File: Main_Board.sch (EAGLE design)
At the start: 54 parts, among them U1 RN4020RN4020, U2 LMS8117, Y1 MC-30632.768K-E3, Y2 MA-5066-25.0000M-C0

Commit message: added jtag
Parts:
- added L1: (no value), SparkFun-Passives:INDUCTOR0805
- added U$11: 1000uF, BB8:CAP_POL_PAN
- added U$12: JTAG, BB8:JTAG
- added U$8: 100uF, BB8:CAP_POL_PAN
- added U3: 5V_BUCK_REG, BB8:5V_BUCK_REG
- added Z1: SCHOTTKY_DIODE, BB8:SCHOTTKY_DIODE
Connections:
- new net N$31: L1.2, U3.OUTPUT, Z1.C
- new net N$32: L1.1, U$11.+, U3.FEEDBACK
- net GND: now also U$11.-, U$8.-, U3.!ON/OFF, U3.GND, Z1.A
- net VCC: now also U$8.+, U3.VIN
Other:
- note added: "double check"
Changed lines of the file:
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@@
 <part name="FRAME4" library="SparkFun-Aesthetics" deviceset="FRAME-LEDGER" device=""/>
 <part name="U2" library="BB8" deviceset="LMS8117" device=""/>
+<part name="U3" library="BB8" deviceset="5V_BUCK_REG" device=""/>
+<part name="SUPPLY20" library="SparkFun-Aesthetics" deviceset="VCC" device=""/>
+<part name="GND32" library="SparkFun-Aesthetics" deviceset="GND" device=""/>
+<part name="U$8" library="BB8" deviceset="CAP_POL_PAN" device="" value="100uF"/>
+<part name="Z1" library="BB8" deviceset="SCHOTTKY_DIODE" device=""/>
+<part name="L1" library="SparkFun-Passives" deviceset="INDUCTOR" device="0805"/>
+<part name="U$11" library="BB8" deviceset="CAP_POL_PAN" device="" value="1000uF"/>
+<part name="GND34" library="SparkFun-Aesthetics" deviceset="GND" device=""/>
+<part name="GND35" library="SparkFun-Aesthetics" deviceset="GND" device=""/>
+<part name="U$12" library="BB8" deviceset="JTAG" device=""/>
 </parts>
 <sheets>
@@
 MC1_INH_3.3
 MC2_INH_3.3</text>
+<text x="35.56" y="-187.96" size="1.778" layer="95">double check</text>
 </plain>
 <instances>
@@
 <instance part="FRAME4" gate="G$2" x="154.94" y="-43.18"/>
 <instance part="U2" gate="G$1" x="-104.14" y="-93.98"/>
+<instance part="U3" gate="G$1" x="-45.72" y="-180.34"/>
+<instance part="SUPPLY20" gate="G$1" x="-76.2" y="-175.26"/>
+<instance part="GND32" gate="1" x="-76.2" y="-208.28"/>
+<instance part="U$8" gate="G$1" x="-101.6" y="-180.34"/>
+<instance part="Z1" gate="G$1" x="-10.16" y="-187.96" rot="R90"/>
+<instance part="L1" gate="G$1" x="5.08" y="-185.42" rot="MR90"/>
+<instance part="U$11" gate="G$1" x="25.4" y="-190.5"/>
+<instance part="GND34" gate="1" x="-10.16" y="-208.28"/>
+<instance part="GND35" gate="1" x="25.4" y="-208.28"/>
+<instance part="U$12" gate="G$1" x="528.32" y="60.96"/>
 </instances>
 <busses>
@@
 <wire x1="7.62" y1="50.8" x2="7.62" y2="48.26" width="0.1524" layer="91"/>
 </segment>
+<segment>
+<pinref part="SUPPLY20" gate="G$1" pin="VCC"/>
+<pinref part="U3" gate="G$1" pin="VIN"/>
+<wire x1="-76.2" y1="-175.26" x2="-76.2" y2="-177.8" width="0.1524" layer="91"/>
+<wire x1="-76.2" y1="-177.8" x2="-60.96" y2="-177.8" width="0.1524" layer="91"/>
+<junction x="-76.2" y="-177.8"/>
+<pinref part="U$8" gate="G$1" pin="+"/>
+<wire x1="-76.2" y1="-177.8" x2="-101.6" y2="-177.8" width="0.1524" layer="91"/>
+</segment>
 </net>
 <net name="GND" class="0">
@@
 <wire x1="304.8" y1="177.8" x2="304.8" y2="175.26" width="0.1524" layer="91"/>
 <pinref part="JP1" gate="G$1" pin="O"/>
+</segment>
+<segment>
+<pinref part="U3" gate="G$1" pin="!ON/OFF"/>
+<pinref part="GND32" gate="1" pin="GND"/>
+<wire x1="-60.96" y1="-182.88" x2="-76.2" y2="-182.88" width="0.1524" layer="91"/>
+<wire x1="-76.2" y1="-182.88" x2="-76.2" y2="-187.96" width="0.1524" layer="91"/>
+<pinref part="U3" gate="G$1" pin="GND"/>
+<wire x1="-76.2" y1="-187.96" x2="-76.2" y2="-205.74" width="0.1524" layer="91"/>
+<wire x1="-60.96" y1="-187.96" x2="-76.2" y2="-187.96" width="0.1524" layer="91"/>
+<junction x="-76.2" y="-187.96"/>
+<pinref part="U$8" gate="G$1" pin="-"/>
+<wire x1="-76.2" y1="-187.96" x2="-101.6" y2="-187.96" width="0.1524" layer="91"/>
+<wire x1="-101.6" y1="-187.96" x2="-101.6" y2="-185.42" width="0.1524" layer="91"/>
+</segment>
+<segment>
+<pinref part="Z1" gate="G$1" pin="A"/>
+<pinref part="GND34" gate="1" pin="GND"/>
+<wire x1="-10.16" y1="-203.2" x2="-10.16" y2="-205.74" width="0.1524" layer="91"/>
+</segment>
+<segment>
+<pinref part="GND35" gate="1" pin="GND"/>
+<wire x1="25.4" y1="-205.74" x2="25.4" y2="-195.58" width="0.1524" layer="91"/>
+<pinref part="U$11" gate="G$1" pin="-"/>
 </segment>
 </net>
@@
 </segment>
 </net>
+<net name="N$31" class="0">
+<segment>
+<pinref part="U3" gate="G$1" pin="OUTPUT"/>
+<pinref part="L1" gate="G$1" pin="2"/>
+<wire x1="-30.48" y1="-185.42" x2="-10.16" y2="-185.42" width="0.1524" layer="91"/>
+<pinref part="Z1" gate="G$1" pin="C"/>
+<wire x1="-10.16" y1="-185.42" x2="-2.54" y2="-185.42" width="0.1524" layer="91"/>
+<wire x1="-10.16" y1="-187.96" x2="-10.16" y2="-185.42" width="0.1524" layer="91"/>
+<junction x="-10.16" y="-185.42"/>
+</segment>
+</net>
+<net name="N$32" class="0">
+<segment>
+<pinref part="L1" gate="G$1" pin="1"/>
+<pinref part="U$11" gate="G$1" pin="+"/>
+<wire x1="12.7" y1="-185.42" x2="25.4" y2="-185.42" width="0.1524" layer="91"/>
+<wire x1="25.4" y1="-185.42" x2="25.4" y2="-187.96" width="0.1524" layer="91"/>
+<pinref part="U3" gate="G$1" pin="FEEDBACK"/>
+<wire x1="-30.48" y1="-177.8" x2="25.4" y2="-177.8" width="0.1524" layer="91"/>
+<wire x1="25.4" y1="-177.8" x2="25.4" y2="-185.42" width="0.1524" layer="91"/>
+<junction x="25.4" y="-185.42"/>
+</segment>
+</net>

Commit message: started adding motors
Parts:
- added J1: (no value), SparkFun-Connectors:M03PTH
- added LED1, LED2, LED3: (no value), LilyPad-Wearables:LED1206
- added R16, R17, R18, R19, R20, R21, R22, R23, R24: 10K, SparkFun-Passives:RESISTOR0805-RES
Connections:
- new net !NRST: S2.O, U$12.NRST, U$5.!RST
- new net BLUE_WAKE_SW: U$5.PA4, U1.WAKE_SW
- new net BLU_CTS: U$5.PA1, U1.PIO5
- new net BLU_RTS: U$5.PA0_WKUP, U1.RTS/PIO6
- new net BLU_RX: U$5.PA2, U1.UART_RX
- new net BLU_TX: U$5.PA3, U1.UART_TX
- new net BLU_WAKE_HW: U$5.PA6, U1.WAKE_HW
- new net JNTRST: U$12.JNTRST, U$5.PB4
- new net JTCK: U$12.JTCK, U$5.PA14
- new net JTDI: U$12.JTDI, U$5.PA15
- new net JTDO: U$12.JTDO, U$5.PB3
- new net JTMS: U$12.JTMS, U$5.PA13
- new net N$33: U1.CMD/MLDP
- new net N$34: R22.2, U1.PIO1
- new net N$35: LED1.A, R22.1
- new net N$36: R23.2, U1.PIO2
- new net N$37: R24.2, U1.PIO3
- new net N$38: LED2.A, R23.1
- new net N$39: LED3.A, R24.1
- new net SERVO_PWM_3.3: U$10.3A, U$5.PA8
- new net SERVO_PWM_5: U$10.3Y
- net 3.3V: now also U$12.VDD, U$12.VDD@2
- net 5V: no longer U$10.3!OE
- net GND: now also LED1.C, LED2.C, LED3.C, R16.1, R17.1, R18.1, R19.1, R20.1, R21.1, U$10.3!OE, U$12.GND, U$12.GND@10, U$12.GND@12, U$12.GND@14, U$12.GND@16, U$12.GND@18, U$12.GND@20, U$12.GND@6, U$12.GND@8; no longer U$10.3A
- net M1_A_3.3: now also U$5.PA7
- net M1_B_3.3: now also U$5.PC4
- net M2_A_3.3: now also U$5.PC5
- net M2_B_3.3: now also U$5.PB0
- net MC1_INH_3.3: now also U$5.PC9
- net MC2_IS: now also U$5.PC1
- net N$24: now also R16.2, U$12.P$11; no longer U$5.PA13
- net N$25: now also R17.2, U$12.P$17; no longer U$5.PA14
- net N$26: now also R18.2, U$12.P$19; no longer U$5.PA15
- net N$27: now also R20.2, U1.AIO1; no longer U$5.PB3
- net N$28: now also R21.2, U1.AIO0; no longer U$5.PB4
- net N$7: now also R19.2, U1.AIO2; no longer S2.O, U$5.!RST
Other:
- note added: "OUTPUT FROM MICRO MC1_IN1 MC1_IN2 MC2_IN1 MC2_IN2"
- moved on the sheet: S2

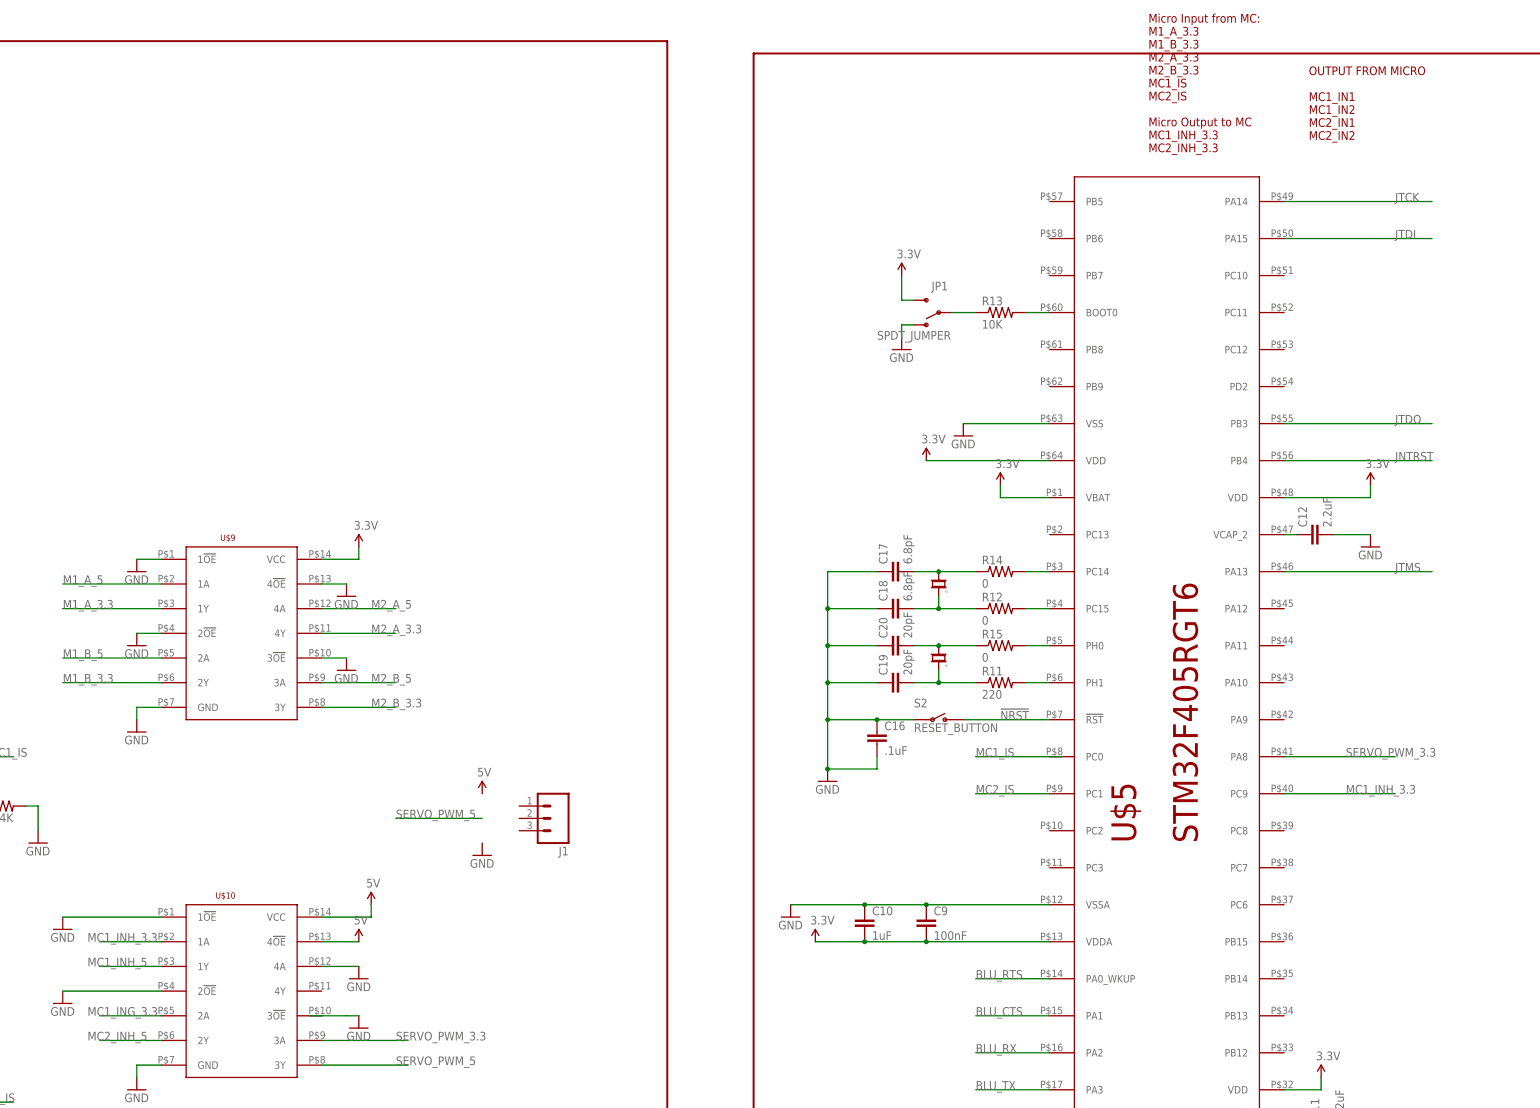
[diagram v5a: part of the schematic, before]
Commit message: finished adding motors
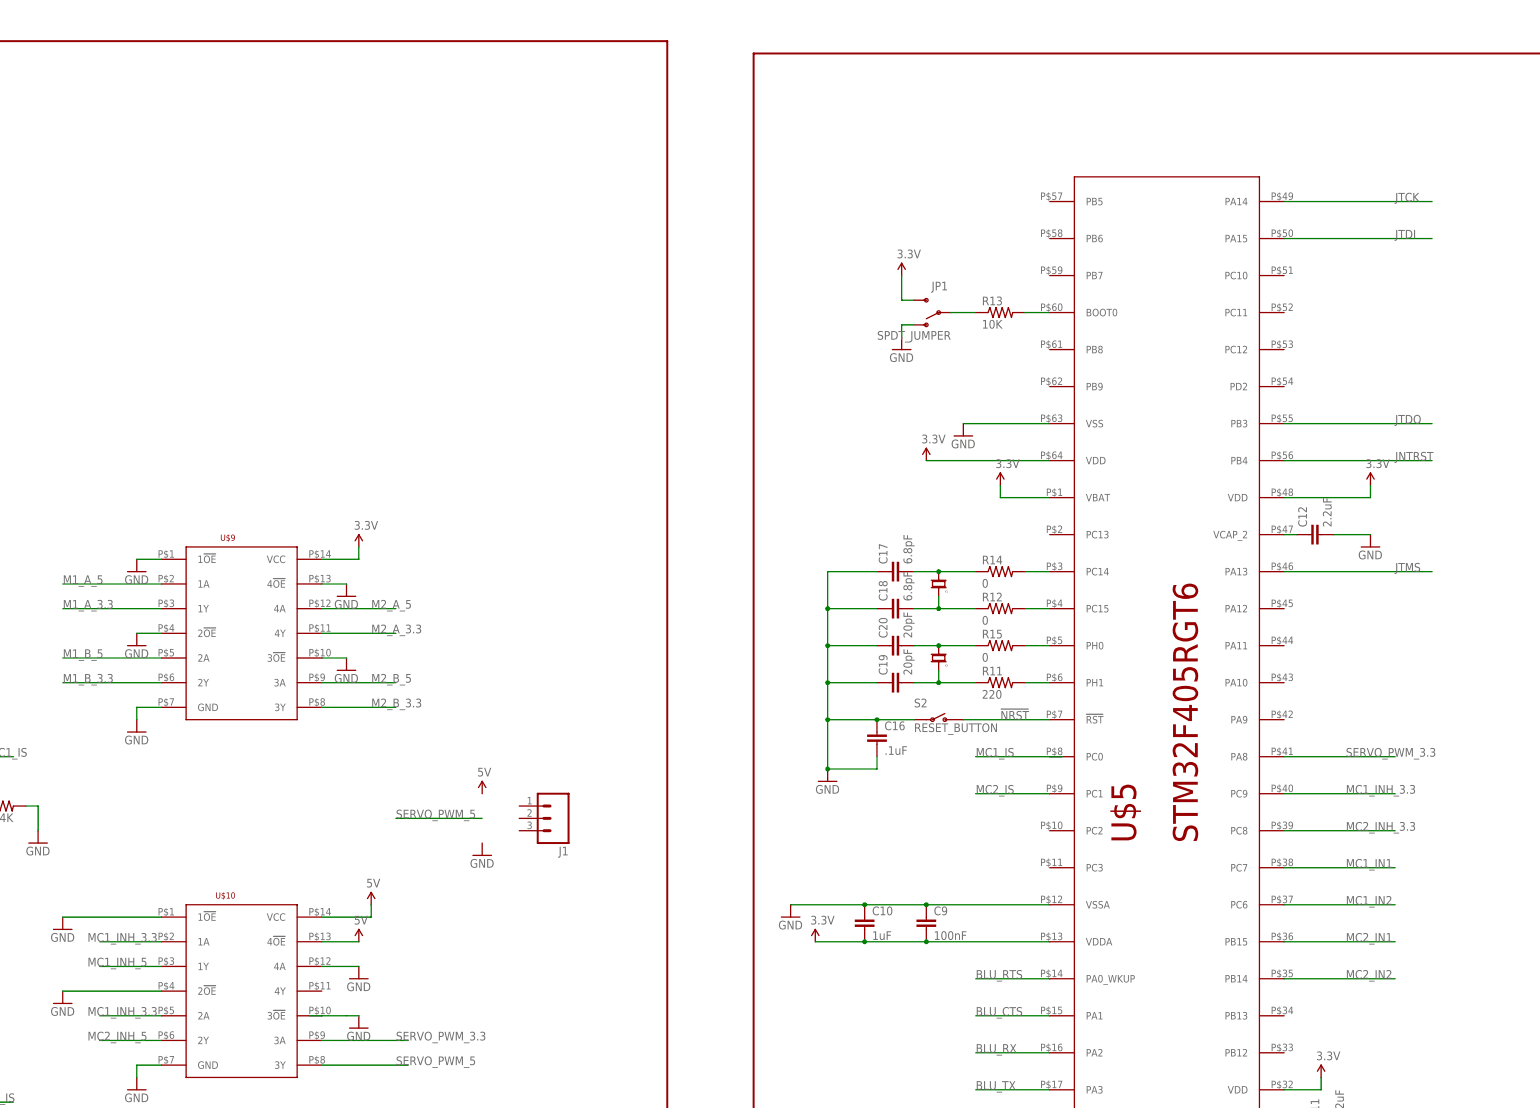
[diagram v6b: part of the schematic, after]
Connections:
- removed net MC1_ING_3.3: U$10.2A
- new net MC2_INH_3.3: U$5.PC8
- net MC1_IN1: now also U$5.PC7
- net MC1_IN2: now also U$5.PC6
- net MC1_INH_3.3: now also U$10.2A
- net MC2_IN1: now also U$5.PB15
- net MC2_IN2: now also U$5.PB14
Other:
- note removed: "Micro Input from MC: M1_A_3.3 M1_B_3.3 M2_A_3.3 M2_B_3.3 MC1_IS MC2_IS Micro Output to MC MC1_INH_3.3 MC2_INH_3.3"
- note removed: "OUTPUT FROM MICRO MC1_IN1 MC1_IN2 MC2_IN1 MC2_IN2"
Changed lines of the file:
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@@
 <text x="7.62" y="-66.04" size="6.4516" layer="95">Power Conversion</text>
 <text x="472.44" y="-71.12" size="6.4516" layer="95">Bluetooth</text>
-<text x="355.6" y="213.36" size="1.778" layer="94">Micro Input from MC:
-M1_A_3.3
-M1_B_3.3
-M2_A_3.3
-M2_B_3.3
-MC1_IS
-MC2_IS
-Micro Output to MC
-MC1_INH_3.3
-MC2_INH_3.3</text>
 <text x="35.56" y="-187.96" size="1.778" layer="95">double check</text>
-<text x="388.62" y="215.9" size="1.778" layer="94">OUTPUT FROM MICRO
-MC1_IN1
-MC1_IN2
-MC2_IN1
-MC2_IN2</text>
 </plain>
 <instances>
@@
 <label x="-15.24" y="30.48" size="1.778" layer="95"/>
 </segment>
+<segment>
+<pinref part="U$5" gate="G$1" pin="PB15"/>
+<wire x1="383.54" y1="50.8" x2="406.4" y2="50.8" width="0.1524" layer="91"/>
+<label x="396.24" y="50.8" size="1.778" layer="95"/>
+</segment>
 </net>
 <net name="MC2_IN2" class="0">
@@
 <label x="-15.24" y="27.94" size="1.778" layer="95"/>
 </segment>
+<segment>
+<pinref part="U$5" gate="G$1" pin="PB14"/>
+<wire x1="383.54" y1="43.18" x2="406.4" y2="43.18" width="0.1524" layer="91"/>
+<label x="396.24" y="43.18" size="1.778" layer="95"/>
+</segment>
 </net>
 <net name="MC1_IN1" class="0">
@@
 <label x="-12.7" y="101.6" size="1.778" layer="95"/>
 </segment>
+<segment>
+<pinref part="U$5" gate="G$1" pin="PC7"/>
+<wire x1="383.54" y1="66.04" x2="406.4" y2="66.04" width="0.1524" layer="91"/>
+<label x="396.24" y="66.04" size="1.778" layer="95"/>
+</segment>
 </net>
 <net name="MC1_IN2" class="0">
@@
 <wire x1="7.62" y1="99.06" x2="-10.16" y2="99.06" width="0.1524" layer="91"/>
 <label x="-12.7" y="99.06" size="1.778" layer="95"/>
+</segment>
+<segment>
+<pinref part="U$5" gate="G$1" pin="PC6"/>
+<wire x1="383.54" y1="58.42" x2="406.4" y2="58.42" width="0.1524" layer="91"/>
+<label x="396.24" y="58.42" size="1.778" layer="95"/>
 </segment>
 </net>
@@
 <label x="396.24" y="81.28" size="1.778" layer="95"/>
 </segment>
-</net>
-<net name="MC1_ING_3.3" class="0">
 <segment>
 <pinref part="U$10" gate="G$1" pin="2A"/>
@@
 </segment>
 </net>
+<net name="MC2_INH_3.3" class="0">
+<segment>
+<pinref part="U$5" gate="G$1" pin="PC8"/>
+<wire x1="383.54" y1="73.66" x2="406.4" y2="73.66" width="0.1524" layer="91"/>
+<label x="396.24" y="73.66" size="1.778" layer="95"/>
+</segment>
+</net>
 </nets>
 </sheet>
@@
 </schematic>
 </drawing>
-<compatibility>
-<note version="6.3" minversion="6.2.2" severity="warning">
-Since Version 6.2.2 text objects can contain more than one line,
-which will not be processed correctly with this version.
-</note>
-</compatibility>
 </eagle>
